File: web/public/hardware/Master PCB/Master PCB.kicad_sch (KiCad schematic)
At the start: 25 parts, among them J1 Rows 0-15, J10 LDR2, J11 LDR3, J12 LDR4, J13 SWD Conn, J14 LED Conn, J15 OLED1, J16 OLED2, J17 Relay Conn, J2 Cols 0-21, J3 Cols 22-31, J4 5V_IN, J5 LED1, J6 LED2, J7 LED3, J8 LED4, J9 LDR1

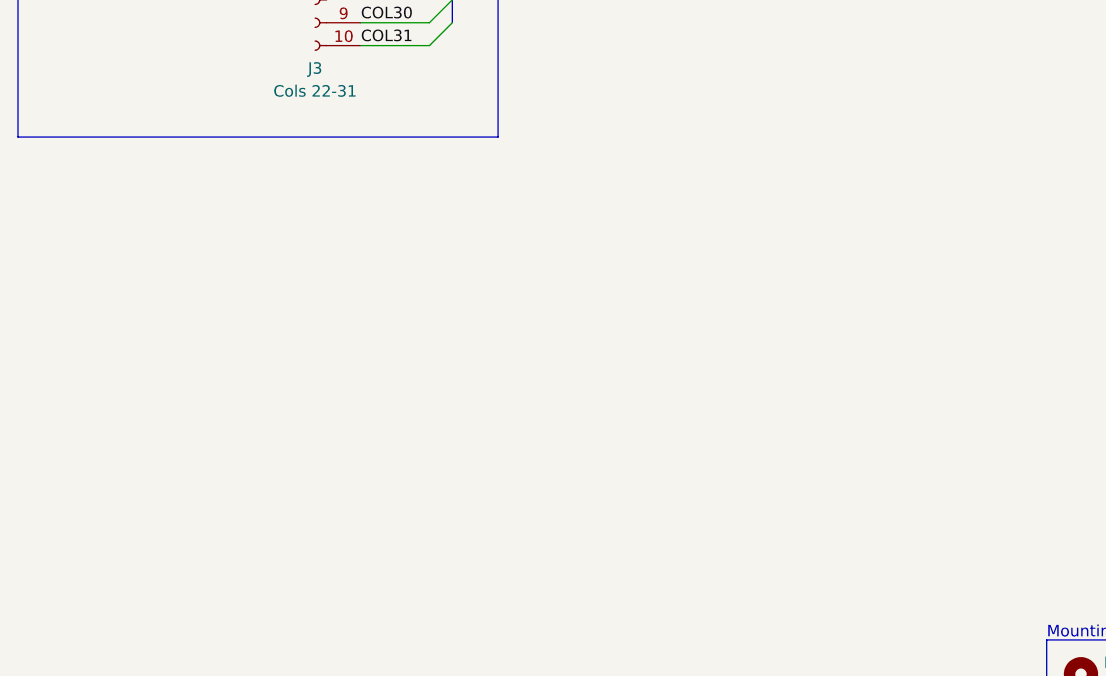
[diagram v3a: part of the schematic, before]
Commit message: Add ESD ICs and route part of board
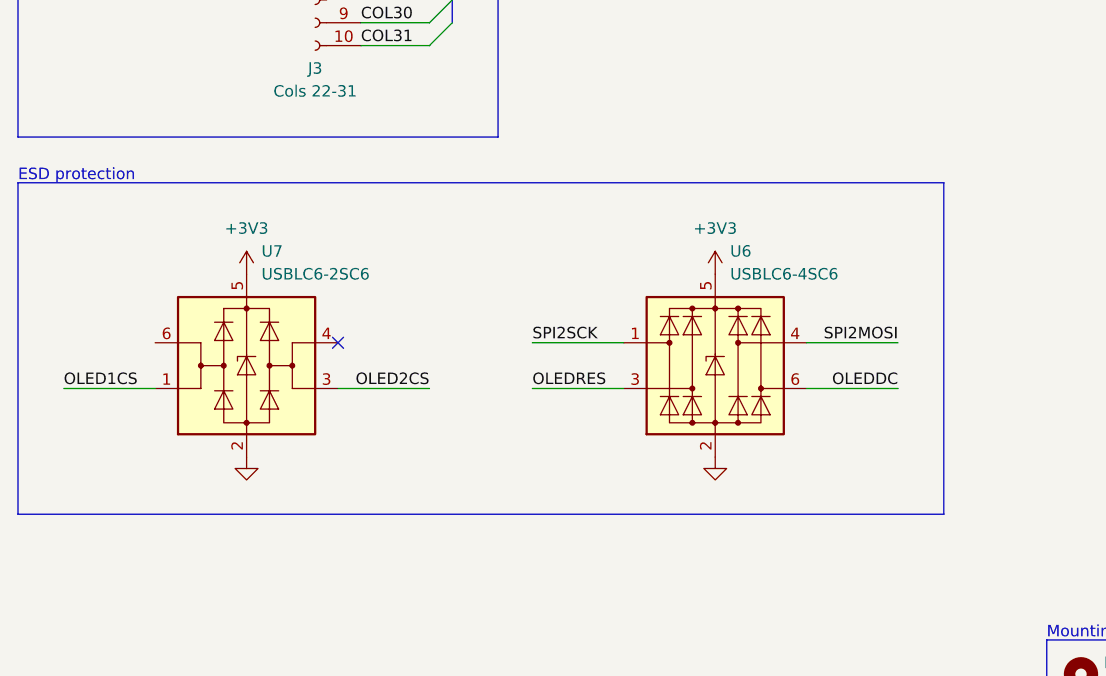
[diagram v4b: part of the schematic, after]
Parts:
- added U6: USBLC6-4SC6, Package_TO_SOT_SMD:SOT-23-6, symbol Power_Protection:USBLC6-4SC6
- added U7: USBLC6-2SC6, Package_TO_SOT_SMD:SOT-23-6, symbol Power_Protection:USBLC6-2SC6
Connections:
- net +3V3: now also U6.5 (VBUS), U7.5 (VBUS)
- net GND: now also U6.2 (GND), U7.2 (GND)
- net OLED1CS: now also U7.1 (I/O1)
- net OLED2CS: now also U7.3 (I/O2)
- net OLEDDC: now also U6.6 (I/O4)
- net OLEDRES: now also U6.3 (I/O2)
- net SPI2MOSI: now also U6.4 (I/O3)
- net SPI2SCK: now also U6.1 (I/O1)
- no-connect marks 0 -> 1
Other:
- note added: "ESD protection"
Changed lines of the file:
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@@
   (junction (at 205.74 115.57) (diameter 0) (color 0 0 0 0)
   )
+  (no_connect (at 53.34 138.43))
   (bus_entry (at 66.04 77.47) (size -2.54 2.54)
     (stroke (width 0) (type default))
@@
     (stroke (width 0) (type default))
   )
+  (wire (pts (xy 74.93 143.51) (xy 85.09 143.51))
+    (stroke (width 0) (type default))
+  )
   (bus (pts (xy 66.04 97.79) (xy 66.04 100.33))
     (stroke (width 0) (type default))
@@
     (stroke (width 0) (type default))
   )
+  (wire (pts (xy 105.41 143.51) (xy 115.57 143.51))
+    (stroke (width 0) (type default))
+  )
   (wire (pts (xy 229.87 102.87) (xy 237.49 102.87))
     (stroke (width 0) (type default))
@@
     (stroke (width 0) (type default))
   )
+  (wire (pts (xy 22.86 143.51) (xy 33.02 143.51))
+    (stroke (width 0) (type default))
+  )
   (wire (pts (xy 121.92 86.36) (xy 121.92 74.93))
     (stroke (width 0) (type default))
@@
     (stroke (width 0) (type default))
   )
+  (wire (pts (xy 53.34 143.51) (xy 63.5 143.51))
+    (stroke (width 0) (type default))
+  )
   (wire (pts (xy 191.77 93.98) (xy 194.31 93.98))
     (stroke (width 0) (type default))
@@
     (stroke (width 0) (type default))
   )
+  (wire (pts (xy 74.93 138.43) (xy 85.09 138.43))
+    (stroke (width 0) (type default))
+  )
   (wire (pts (xy 220.98 107.95) (xy 220.98 133.35))
     (stroke (width 0) (type default))
@@
     (stroke (width 0) (type default))
   )
+  (wire (pts (xy 105.41 138.43) (xy 115.57 138.43))
+    (stroke (width 0) (type default))
+  )
   (bus (pts (xy 66.04 26.67) (xy 66.04 29.21))
     (stroke (width 0) (type default))
@@
     (fill (type none))
   )
+  (rectangle (start 17.78 120.65) (end 120.65 157.48)
+    (stroke (width 0) (type default))
+    (fill (type none))
+  )
   (rectangle (start 17.78 177.8) (end 67.31 198.12)
     (stroke (width 0) (type default))
@@
     (effects (font (size 1.27 1.27)) (justify left bottom))
   )
+  (text "ESD protection" (at 17.78 120.65 0)
+    (effects (font (size 1.27 1.27)) (justify left bottom))
+  )
   (text "OLED headers" (at 223.52 93.98 0)
     (effects (font (size 1.27 1.27)) (justify left bottom))
@@
     (effects (font (size 1.27 1.27)) (justify left bottom))
   )
+  (label "OLEDRES" (at 74.93 143.51 0) (fields_autoplaced)
+    (effects (font (size 1.27 1.27)) (justify left bottom))
+  )
   (label "COL5" (at 55.88 39.37 0) (fields_autoplaced)
     (effects (font (size 1.27 1.27)) (justify left bottom))
   )
   (label "ROW8" (at 30.48 46.99 0) (fields_autoplaced)
+    (effects (font (size 1.27 1.27)) (justify left bottom))
+  )
+  (label "OLED1CS" (at 22.86 143.51 0) (fields_autoplaced)
     (effects (font (size 1.27 1.27)) (justify left bottom))
   )
@@
     (effects (font (size 1.27 1.27)) (justify right bottom))
   )
+  (label "OLEDDC" (at 115.57 143.51 180) (fields_autoplaced)
+    (effects (font (size 1.27 1.27)) (justify right bottom))
+  )
   (label "SPI2SCK" (at 227.33 107.95 0) (fields_autoplaced)
     (effects (font (size 1.27 1.27)) (justify left bottom))
@@
     (effects (font (size 1.27 1.27)) (justify left bottom))
   )
+  (label "SPI2SCK" (at 74.93 138.43 0) (fields_autoplaced)
+    (effects (font (size 1.27 1.27)) (justify left bottom))
+  )
   (label "COL12" (at 55.88 57.15 0) (fields_autoplaced)
     (effects (font (size 1.27 1.27)) (justify left bottom))
@@
     (effects (font (size 1.27 1.27)) (justify left bottom))
   )
+  (label "SPI2MOSI" (at 115.57 138.43 180) (fields_autoplaced)
+    (effects (font (size 1.27 1.27)) (justify right bottom))
+  )
   (label "ROW14" (at 30.48 62.23 0) (fields_autoplaced)
     (effects (font (size 1.27 1.27)) (justify left bottom))
@@
   (label "COL[0..31]" (at 147.32 59.69 0) (fields_autoplaced)
     (effects (font (size 1.27 1.27)) (justify left bottom))
+  )
+  (label "OLED2CS" (at 63.5 143.51 180) (fields_autoplaced)
+    (effects (font (size 1.27 1.27)) (justify right bottom))
   )
   (label "ROW7" (at 30.48 44.45 0) (fields_autoplaced)
@@
     )
   )
+  (symbol (lib_id "Power_Protection:USBLC6-4SC6") (at 95.25 140.97 0) (unit 1)
+    (in_bom yes) (on_board yes) (dnp no) (fields_autoplaced)
+    (property "Reference" "U6" (at 96.9011 128.27 0)
+      (effects (font (size 1.27 1.27)) (justify left))
+    )
+    (property "Value" "USBLC6-4SC6" (at 96.9011 130.81 0)
+      (effects (font (size 1.27 1.27)) (justify left))
+    )
+    (property "Footprint" "Package_TO_SOT_SMD:SOT-23-6" (at 95.25 153.67 0)
+      (effects (font (size 1.27 1.27)) hide)
+    )
+    (property "Datasheet" "https://www.st.com/resource/en/datasheet/usblc6-4.pdf" (at 100.33 132.08 0)
+      (effects (font (size 1.27 1.27)) hide)
+    )
+    (pin "1")
+    (pin "2")
+    (pin "3")
+    (pin "4")
+    (pin "5")
+    (pin "6")
+    (instances
+      (project "Master PCB"
+        (path "/61606422-4f73-4717-9ce6-6ac5e634e7ae"
+          (reference "U6") (unit 1)
+        )
+      )
+    )
+  )
   (symbol (lib_id "power:+3V3") (at 234.95 125.73 0) (unit 1)
     (in_bom yes) (on_board yes) (dnp no)
@@
         (path "/61606422-4f73-4717-9ce6-6ac5e634e7ae"
           (reference "#PWR024") (unit 1)
+        )
+      )
+    )
+  )
+  (symbol (lib_id "power:+3V3") (at 43.18 130.81 0) (unit 1)
+    (in_bom yes) (on_board yes) (dnp no) (fields_autoplaced)
+    (property "Reference" "#PWR082" (at 43.18 134.62 0)
+      (effects (font (size 1.27 1.27)) hide)
+    )
+    (property "Value" "+3V3" (at 43.18 125.73 0)
+      (effects (font (size 1.27 1.27)))
+    )
+    (property "Footprint" "" (at 43.18 130.81 0)
+      (effects (font (size 1.27 1.27)) hide)
+    )
+    (property "Datasheet" "" (at 43.18 130.81 0)
+      (effects (font (size 1.27 1.27)) hide)
+    )
+    (pin "1")
+    (instances
+      (project "Master PCB"
+        (path "/61606422-4f73-4717-9ce6-6ac5e634e7ae"
+          (reference "#PWR082") (unit 1)
         )
       )
@@
         (path "/61606422-4f73-4717-9ce6-6ac5e634e7ae"
           (reference "J1") (unit 1)
+        )
+      )
+    )
+  )
+  (symbol (lib_id "power:+3V3") (at 95.25 130.81 0) (unit 1)
+    (in_bom yes) (on_board yes) (dnp no) (fields_autoplaced)
+    (property "Reference" "#PWR079" (at 95.25 134.62 0)
+      (effects (font (size 1.27 1.27)) hide)
+    )
+    (property "Value" "+3V3" (at 95.25 125.73 0)
+      (effects (font (size 1.27 1.27)))
+    )
+    (property "Footprint" "" (at 95.25 130.81 0)
+      (effects (font (size 1.27 1.27)) hide)
+    )
+    (property "Datasheet" "" (at 95.25 130.81 0)
+      (effects (font (size 1.27 1.27)) hide)
+    )
+    (pin "1")
+    (instances
+      (project "Master PCB"
+        (path "/61606422-4f73-4717-9ce6-6ac5e634e7ae"
+          (reference "#PWR079") (unit 1)
         )
       )
@@
     )
   )
+  (symbol (lib_id "power:GND") (at 43.18 151.13 0) (unit 1)
+    (in_bom yes) (on_board yes) (dnp no) (fields_autoplaced)
+    (property "Reference" "#PWR083" (at 43.18 157.48 0)
+      (effects (font (size 1.27 1.27)) hide)
+    )
+    (property "Value" "GND" (at 43.18 156.21 0)
+      (effects (font (size 1.27 1.27)) hide)
+    )
+    (property "Footprint" "" (at 43.18 151.13 0)
+      (effects (font (size 1.27 1.27)) hide)
+    )
+    (property "Datasheet" "" (at 43.18 151.13 0)
+      (effects (font (size 1.27 1.27)) hide)
+    )
+    (pin "1")
+    (instances
+      (project "Master PCB"
+        (path "/61606422-4f73-4717-9ce6-6ac5e634e7ae"
+          (reference "#PWR083") (unit 1)
+        )
+      )
+    )
+  )
+  (symbol (lib_id "Power_Protection:USBLC6-2SC6") (at 43.18 140.97 0) (unit 1)
+    (in_bom yes) (on_board yes) (dnp no) (fields_autoplaced)
+    (property "Reference" "U7" (at 44.8311 128.27 0)
+      (effects (font (size 1.27 1.27)) (justify left))
+    )
+    (property "Value" "USBLC6-2SC6" (at 44.8311 130.81 0)
+      (effects (font (size 1.27 1.27)) (justify left))
+    )
+    (property "Footprint" "Package_TO_SOT_SMD:SOT-23-6" (at 43.18 153.67 0)
+      (effects (font (size 1.27 1.27)) hide)
+    )
+    (property "Datasheet" "https://www.st.com/resource/en/datasheet/usblc6-2.pdf" (at 48.26 132.08 0)
+      (effects (font (size 1.27 1.27)) hide)
+    )
+    (pin "1")
+    (pin "2")
+    (pin "3")
+    (pin "4")
+    (pin "5")
+    (pin "6")
+    (instances
+      (project "Master PCB"
+        (path "/61606422-4f73-4717-9ce6-6ac5e634e7ae"
+          (reference "U7") (unit 1)
+        )
+      )
+    )
+  )
   (symbol (lib_id "Device:R_Small_US") (at 90.17 43.18 270) (mirror x) (unit 1)
     (in_bom yes) (on_board yes) (dnp no)
@@
         )
       )
+    )
+  )
+  (symbol (lib_id "power:GND") (at 95.25 151.13 0) (unit 1)
+    (in_bom yes) (on_board yes) (dnp no) (fields_autoplaced)
+    (property "Reference" "#PWR080" (at 95.25 157.48 0)
+      (effects (font (size 1.27 1.27)) hide)
+    )
+    (property "Value" "GND" (at 95.25 156.21 0)
+      (effects (font (size 1.27 1.27)) hide)
+    )
+    (property "Footprint" "" (at 95.25 151.13 0)
+      (effects (font (size 1.27 1.27)) hide)
+    )
+    (property "Datasheet" "" (at 95.25 151.13 0)
+      (effects (font (size 1.27 1.27)) hide)
+    )
+    (pin "1")
+    (instances
+      (project "Master PCB"
+        (path "/61606422-4f73-4717-9ce6-6ac5e634e7ae"
+          (reference "#PWR080") (unit 1)
+        )
+      )

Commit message: Finish routing
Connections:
- net OLEDDC: now also U6.4 (I/O3); no longer U6.6 (I/O4)
- net OLEDRES: now also U6.6 (I/O4); no longer U6.3 (I/O2)
- net SPI2MOSI: now also U6.3 (I/O2); no longer U6.4 (I/O3)
- no-connect marks 1 -> 2
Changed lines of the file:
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@@
   )
   (no_connect (at 53.34 138.43))
+  (no_connect (at 33.02 138.43))
   (bus_entry (at 66.04 77.47) (size -2.54 2.54)
     (stroke (width 0) (type default))
@@
     (effects (font (size 1.27 1.27)) (justify left bottom))
   )
-  (label "OLEDRES" (at 74.93 143.51 0) (fields_autoplaced)
-    (effects (font (size 1.27 1.27)) (justify left bottom))
+  (label "OLEDRES" (at 115.57 143.51 180) (fields_autoplaced)
+    (effects (font (size 1.27 1.27)) (justify right bottom))
   )
   (label "COL5" (at 55.88 39.37 0) (fields_autoplaced)
@@
     (effects (font (size 1.27 1.27)) (justify right bottom))
   )
-  (label "OLEDDC" (at 115.57 143.51 180) (fields_autoplaced)
+  (label "OLEDDC" (at 115.57 138.43 180) (fields_autoplaced)
     (effects (font (size 1.27 1.27)) (justify right bottom))
   )
@@
     (effects (font (size 1.27 1.27)) (justify left bottom))
   )
-  (label "SPI2MOSI" (at 115.57 138.43 180) (fields_autoplaced)
-    (effects (font (size 1.27 1.27)) (justify right bottom))
+  (label "SPI2MOSI" (at 74.93 143.51 0) (fields_autoplaced)
+    (effects (font (size 1.27 1.27)) (justify left bottom))
   )
   (label "ROW14" (at 30.48 62.23 0) (fields_autoplaced)

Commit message: Update labels
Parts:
- added D5, D6: GRN, LED_SMD:LED_0805_2012Metric_Pad1.15x1.40mm_HandSolder, symbol Device:LED_Small
- added R26, R3: 100, Resistor_SMD:R_0805_2012Metric_Pad1.20x1.40mm_HandSolder, symbol Device:R_Small_US
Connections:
- net +3V3: now also D6.2 (A)
- net +5V: now also D5.2 (A)
- net GND: now also R26.2, R3.2
- new net: D6.1 (K), R26.1
- new net: D5.1 (K), R3.1
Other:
- note added: "Power LEDs"
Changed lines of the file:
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@@
+    (fill (type none))
+  )
+  (rectangle (start 72.39 175.26) (end 97.79 198.12)
+    (stroke (width 0) (type default))
     (fill (type none))
   )
@@
     (effects (font (size 1.27 1.27)) (justify left bottom))
   )
+  (text "Power LEDs" (at 72.39 175.26 0)
+    (effects (font (size 1.27 1.27)) (justify left bottom))
+  )
   (text "OLED headers" (at 223.52 93.98 0)
     (effects (font (size 1.27 1.27)) (justify left bottom))
@@
         (path "/61606422-4f73-4717-9ce6-6ac5e634e7ae"
           (reference "J14") (unit 1)
+        )
+      )
+    )
+  )
+  (symbol (lib_id "power:GND") (at 88.9 193.04 0) (unit 1)
+    (in_bom yes) (on_board yes) (dnp no) (fields_autoplaced)
+    (property "Reference" "#PWR091" (at 88.9 199.39 0)
+      (effects (font (size 1.27 1.27)) hide)
+    )
+    (property "Value" "GND" (at 88.9 198.12 0)
+      (effects (font (size 1.27 1.27)) hide)
+    )
+    (property "Footprint" "" (at 88.9 193.04 0)
+      (effects (font (size 1.27 1.27)) hide)
+    )
+    (property "Datasheet" "" (at 88.9 193.04 0)
+      (effects (font (size 1.27 1.27)) hide)
+    )
+    (pin "1")
+    (instances
+      (project "Master PCB"
+        (path "/61606422-4f73-4717-9ce6-6ac5e634e7ae"
+          (reference "#PWR091") (unit 1)
         )
       )
@@
     )
   )
+  (symbol (lib_id "Device:LED_Small") (at 88.9 185.42 90) (unit 1)
+    (in_bom yes) (on_board yes) (dnp no)
+    (property "Reference" "D6" (at 91.44 184.0865 90)
+      (effects (font (size 1.27 1.27)) (justify right))
+    )
+    (property "Value" "GRN" (at 91.44 186.6265 90)
+      (effects (font (size 1.27 1.27)) (justify right))
+    )
+    (property "Footprint" "LED_SMD:LED_0805_2012Metric_Pad1.15x1.40mm_HandSolder" (at 88.9 185.42 90)
+      (effects (font (size 1.27 1.27)) hide)
+    )
+    (property "Datasheet" "~" (at 88.9 185.42 90)
+      (effects (font (size 1.27 1.27)) hide)
+    )
+    (pin "1")
+    (pin "2")
+    (instances
+      (project "Master PCB"
+        (path "/61606422-4f73-4717-9ce6-6ac5e634e7ae"
+          (reference "D6") (unit 1)
+        )
+      )
+    )
+  )
   (symbol (lib_id "Connector:Conn_01x02_Socket") (at 85.09 71.12 0) (mirror y) (unit 1)
     (in_bom yes) (on_board yes) (dnp no)
@@
         (path "/61606422-4f73-4717-9ce6-6ac5e634e7ae"
           (reference "#PWR030") (unit 1)
+        )
+      )
+    )
+  )
+  (symbol (lib_id "Device:R_Small_US") (at 77.47 190.5 0) (unit 1)
+    (in_bom yes) (on_board yes) (dnp no) (fields_autoplaced)
+    (property "Reference" "R3" (at 80.01 189.23 0)
+      (effects (font (size 1.27 1.27)) (justify left))
+    )
+    (property "Value" "100" (at 80.01 191.77 0)
+      (effects (font (size 1.27 1.27)) (justify left))
+    )
+    (property "Footprint" "Resistor_SMD:R_0805_2012Metric_Pad1.20x1.40mm_HandSolder" (at 77.47 190.5 0)
+      (effects (font (size 1.27 1.27)) hide)
+    )
+    (property "Datasheet" "~" (at 77.47 190.5 0)
+      (effects (font (size 1.27 1.27)) hide)
+    )
+    (pin "1")
+    (pin "2")
+    (instances
+      (project "Master PCB"
+        (path "/61606422-4f73-4717-9ce6-6ac5e634e7ae"
+          (reference "R3") (unit 1)
         )
       )
@@
     )
   )
+  (symbol (lib_id "power:+3V3") (at 88.9 182.88 0) (unit 1)
+    (in_bom yes) (on_board yes) (dnp no) (fields_autoplaced)
+    (property "Reference" "#PWR039" (at 88.9 186.69 0)
+      (effects (font (size 1.27 1.27)) hide)
+    )
+    (property "Value" "+3V3" (at 88.9 177.8 0)
+      (effects (font (size 1.27 1.27)))
+    )
+    (property "Footprint" "" (at 88.9 182.88 0)
+      (effects (font (size 1.27 1.27)) hide)
+    )
+    (property "Datasheet" "" (at 88.9 182.88 0)
+      (effects (font (size 1.27 1.27)) hide)
+    )
+    (pin "1")
+    (instances
+      (project "Master PCB"
+        (path "/61606422-4f73-4717-9ce6-6ac5e634e7ae"
+          (reference "#PWR039") (unit 1)
+        )
+      )
+    )
+  )
+  (symbol (lib_id "Device:R_Small_US") (at 88.9 190.5 0) (unit 1)
+    (in_bom yes) (on_board yes) (dnp no) (fields_autoplaced)
+    (property "Reference" "R26" (at 91.44 189.23 0)
+      (effects (font (size 1.27 1.27)) (justify left))
+    )
+    (property "Value" "100" (at 91.44 191.77 0)
+      (effects (font (size 1.27 1.27)) (justify left))
+    )
+    (property "Footprint" "Resistor_SMD:R_0805_2012Metric_Pad1.20x1.40mm_HandSolder" (at 88.9 190.5 0)
+      (effects (font (size 1.27 1.27)) hide)
+    )
+    (property "Datasheet" "~" (at 88.9 190.5 0)
+      (effects (font (size 1.27 1.27)) hide)
+    )
+    (pin "1")
+    (pin "2")
+    (instances
+      (project "Master PCB"
+        (path "/61606422-4f73-4717-9ce6-6ac5e634e7ae"
+          (reference "R26") (unit 1)
+        )
+      )
+    )
+  )
   (symbol (lib_id "Connector:Conn_01x07_Pin") (at 242.57 135.89 0) (mirror y) (unit 1)
     (in_bom yes) (on_board yes) (dnp no) (fields_autoplaced)
@@
         (path "/61606422-4f73-4717-9ce6-6ac5e634e7ae"
           (reference "J6") (unit 1)
+        )
+      )
+    )
+  )
+  (symbol (lib_id "power:+5V") (at 77.47 182.88 0) (unit 1)
+    (in_bom yes) (on_board yes) (dnp no) (fields_autoplaced)
+    (property "Reference" "#PWR033" (at 77.47 186.69 0)
+      (effects (font (size 1.27 1.27)) hide)
+    )
+    (property "Value" "+5V" (at 77.47 177.8 0)
+      (effects (font (size 1.27 1.27)))
+    )
+    (property "Footprint" "" (at 77.47 182.88 0)
+      (effects (font (size 1.27 1.27)) hide)
+    )
+    (property "Datasheet" "" (at 77.47 182.88 0)
+      (effects (font (size 1.27 1.27)) hide)
+    )
+    (pin "1")
+    (instances
+      (project "Master PCB"
+        (path "/61606422-4f73-4717-9ce6-6ac5e634e7ae"
+          (reference "#PWR033") (unit 1)
         )
       )
@@
     )
   )
+  (symbol (lib_id "power:GND") (at 77.47 193.04 0) (unit 1)
+    (in_bom yes) (on_board yes) (dnp no) (fields_autoplaced)
+    (property "Reference" "#PWR090" (at 77.47 199.39 0)
+      (effects (font (size 1.27 1.27)) hide)
+    )
+    (property "Value" "GND" (at 77.47 198.12 0)
+      (effects (font (size 1.27 1.27)) hide)
+    )
+    (property "Footprint" "" (at 77.47 193.04 0)
+      (effects (font (size 1.27 1.27)) hide)
+    )
+    (property "Datasheet" "" (at 77.47 193.04 0)
+      (effects (font (size 1.27 1.27)) hide)
+    )
+    (pin "1")
+    (instances
+      (project "Master PCB"
+        (path "/61606422-4f73-4717-9ce6-6ac5e634e7ae"
+          (reference "#PWR090") (unit 1)
+        )
+      )
+    )
+  )
   (symbol (lib_id "Mechanical:MountingHole") (at 135.89 181.61 0) (unit 1)
     (in_bom yes) (on_board yes) (dnp no)
@@
         )
       )
+    )
+  )
+  (symbol (lib_id "Device:LED_Small") (at 77.47 185.42 90) (unit 1)
+    (in_bom yes) (on_board yes) (dnp no) (fields_autoplaced)
+    (property "Reference" "D5" (at 80.01 184.0865 90)
+      (effects (font (size 1.27 1.27)) (justify right))
+    )
+    (property "Value" "GRN" (at 80.01 186.6265 90)
+      (effects (font (size 1.27 1.27)) (justify right))
+    )
+    (property "Footprint" "LED_SMD:LED_0805_2012Metric_Pad1.15x1.40mm_HandSolder" (at 77.47 185.42 90)
+      (effects (font (size 1.27 1.27)) hide)
+    )
+    (property "Datasheet" "~" (at 77.47 185.42 90)
+      (effects (font (size 1.27 1.27)) hide)
+    )
+    (pin "1")
+    (pin "2")
+    (instances
+      (project "Master PCB"
+        (path "/61606422-4f73-4717-9ce6-6ac5e634e7ae"
+          (reference "D5") (unit 1)
+        )
+      )
